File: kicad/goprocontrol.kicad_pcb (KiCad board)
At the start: 2 copper layers, 45.7 x 49.8 mm, 23 parts, among them P1 CONN_01X02, P2 CONN_01X06, Q1 IRLML6344, SW1 Reset, SW2 Prog, U1 LTV-814, U2 ESP-12E, U3 D24V5F3

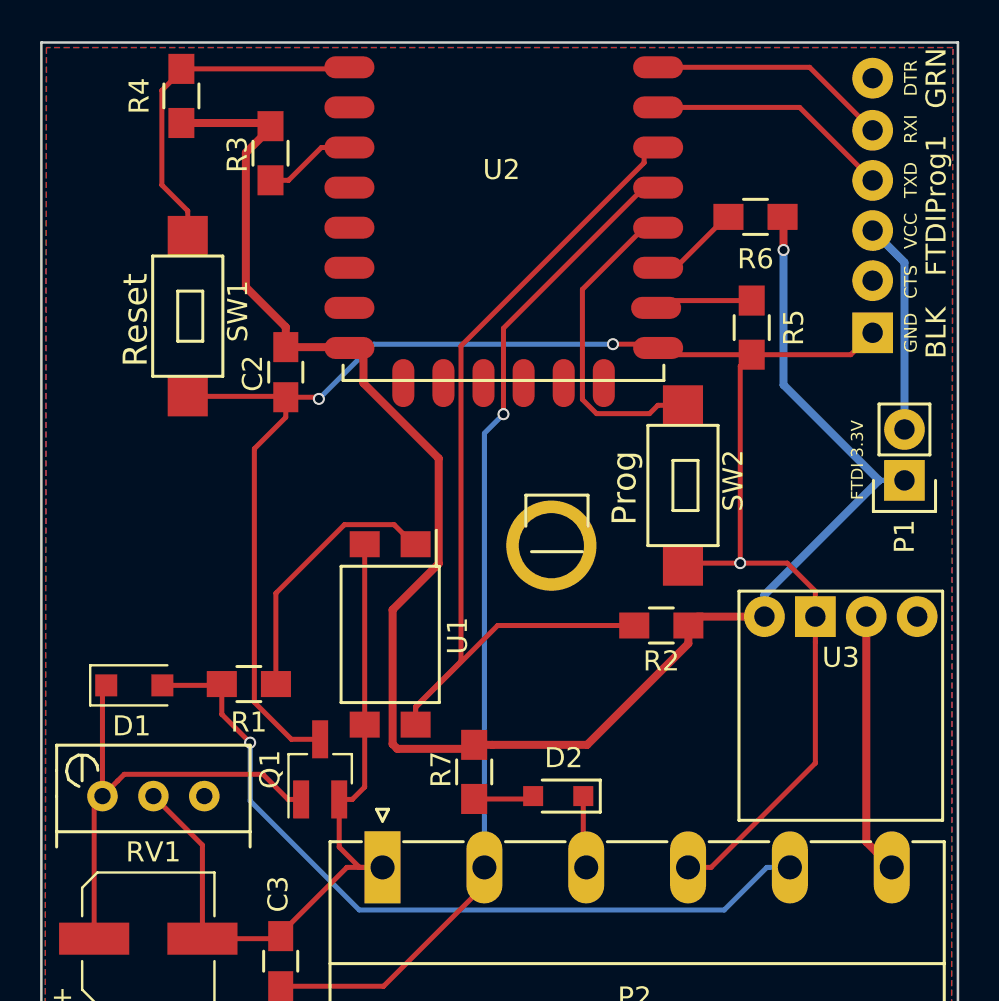
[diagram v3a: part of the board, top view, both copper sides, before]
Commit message: v2.3 Board
- Larger holes for 1x6 connector
- Move 3.3V regulator out of the way
- clean up traces
- remove 3.3V FTDI selector
- Move Prog switch
- Better GND/SW-GND for MOSFET
- Add status LED
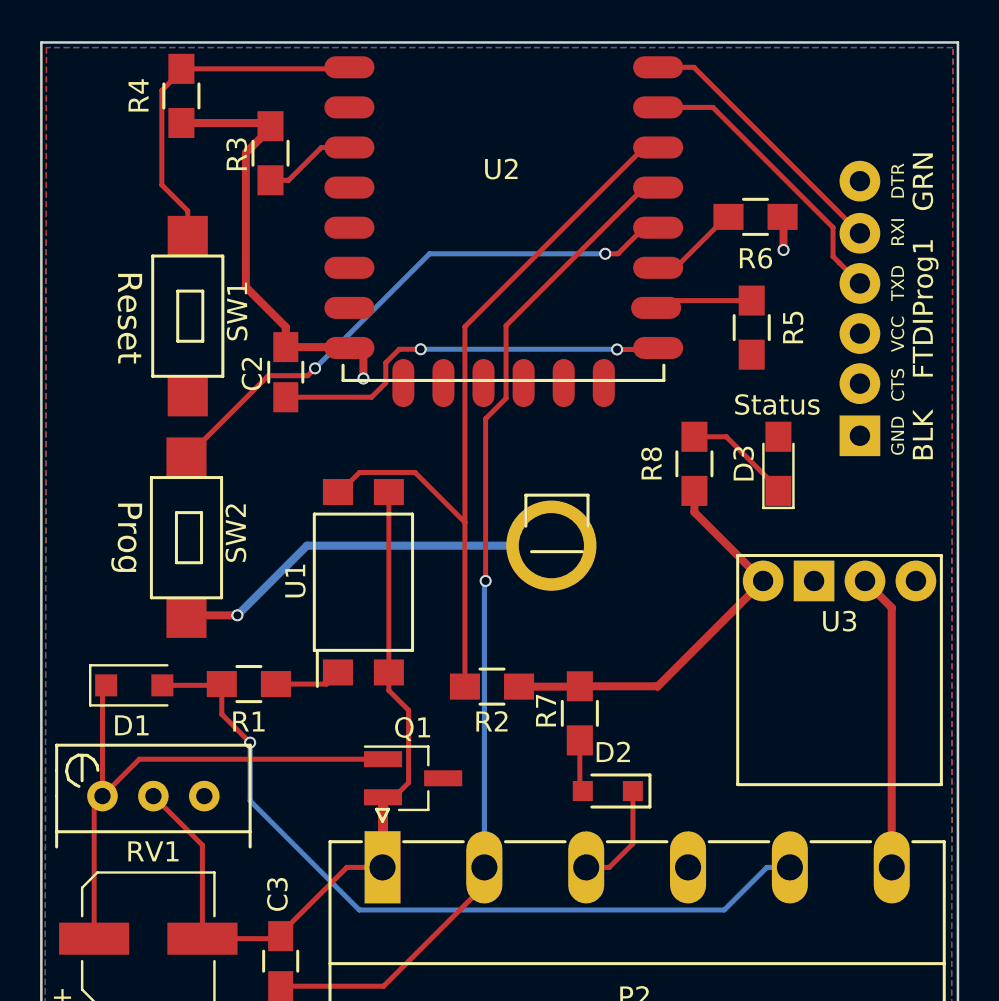
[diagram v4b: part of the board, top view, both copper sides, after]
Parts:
- removed P1: CONN_01X02, Pin_Headers:Pin_Header_Straight_1x02
- added D3: Red, LEDs:LED_0805_HandSoldering, F.Cu at (199.3, 109.9)
- added R8: 56, Resistors_SMD:R_0805_HandSoldering, F.Cu at (195.1, 109.9)
- P2: footprint Connectors_Phoenix:PhoenixContact_MC-G_06x5.08mm_Angled -> PhoenixContact_MC-G_06x5.08mm_Angled
- moved SW2 24.9 mm to (169.8, 113.6)
- moved R2 8.98 mm to (185.0, 121.0)
- moved R7 6.03 mm to (189.4, 122.4)
- moved FTDIProg1 5.18 mm to (203.4, 102.2)
- moved Q1 4.66 mm to (181.1, 125.6), turned to 0 degrees
- moved U1 2.93 mm to (178.6, 115.8), turned to 90 degrees
- moved D2 2.49 mm to (190.8, 126.2)
- moved U3 1.78 mm to (207.5, 118.3)
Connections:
- FTDIProg1 pad 4: Net-(FTDIProg1-Pad4) -> (no net)
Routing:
- net SwitchedGnd: track 91.0 -> 39.2 mm
- net +3V3: track 91.8 -> 44.2 mm, vias 1 -> 2
- net Net-(SW2-Pad1): track 15.3 -> 27.6 mm, vias 0 -> 2
- net Net-(FTDIProg1-Pad4): track 10.6 -> 0.00 mm
- net Net-(R1-Pad1): track 13.3 -> 3.34 mm
- net GPIO5: track 47.1 -> 38.5 mm
- net Net-(D3-Pad1): track 0.00 -> 5.37 mm
- net Net-(C1-Pad1): track 23.8 -> 27.6 mm
- net RXD: track 12.9 -> 15.2 mm
- net LoggerTrigger: track 3.62 -> 5.66 mm
- net +12V: track 13.0 -> 14.8 mm
- net TXD: track 12.7 -> 14.2 mm
- net GND: track 37.3 -> 38.6 mm
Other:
- board text added: "GoProControl v2.3 https://synfin.net/goprocontrol"
- board text added: "Status"
- board text removed: "FTDI 3.3V"
- board text removed: "GoProControl v2.2 https://synfin.net/goprocontrol"

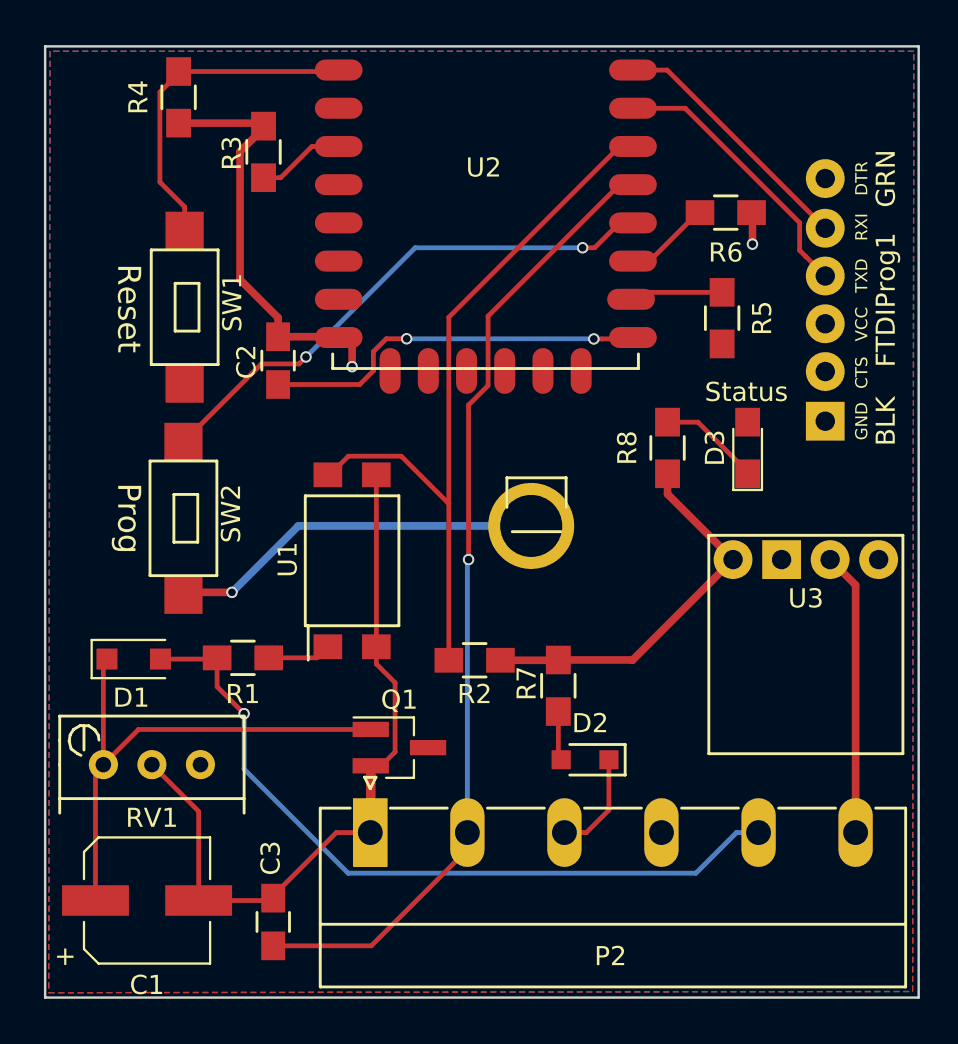
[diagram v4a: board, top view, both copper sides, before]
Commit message: v2.5 of the board
- Move main connector to front
- Use MOSFET to drive GPIO12 like MXL2
- Larger traces for Switched Ground
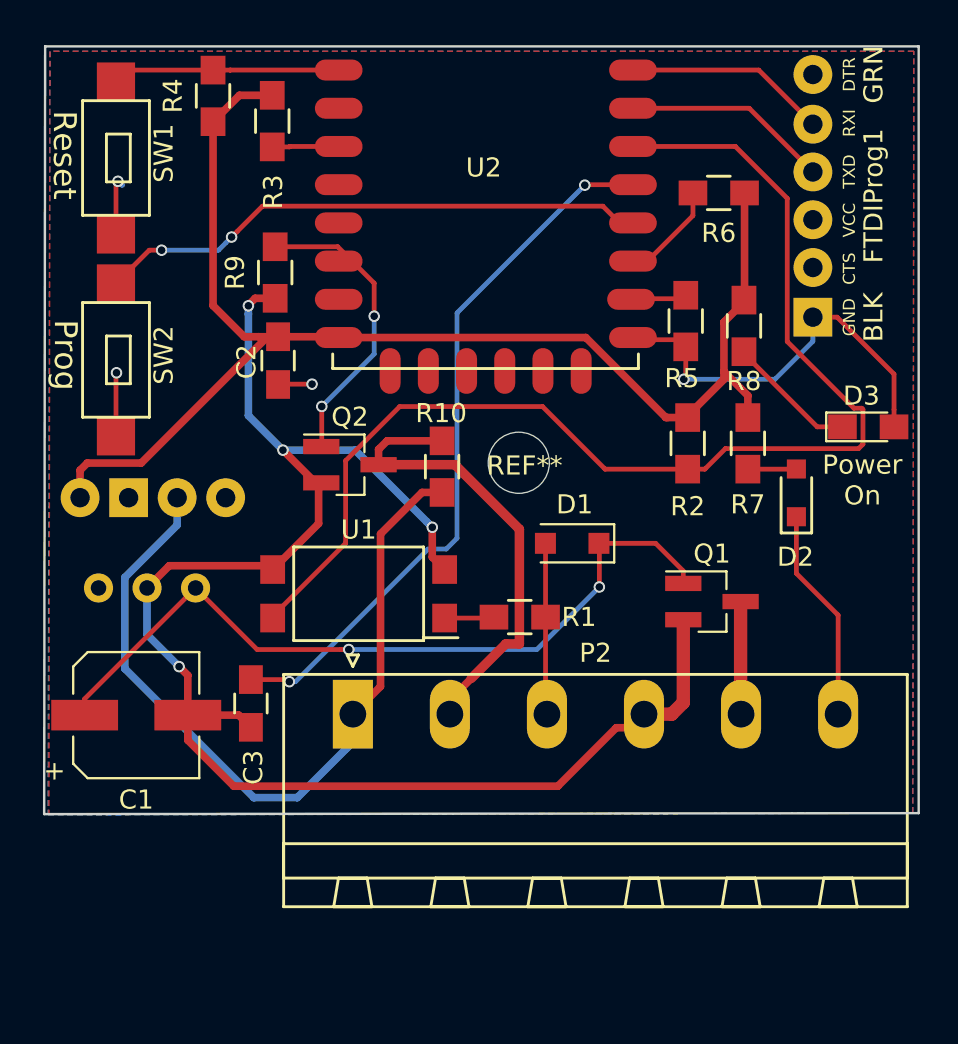
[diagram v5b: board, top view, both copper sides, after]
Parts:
- removed ?: Pin_Header_Straight_1x01, Pin_Headers:Pin_Header_Straight_1x01
- added Q2: IRLML6344, TO_SOT_Packages_SMD:SOT-23_Handsoldering, F.Cu at (178.5, 110.8)
- added R10: 10K, Resistors_SMD:R_0805_HandSoldering, F.Cu at (183.3, 110.9)
- added R9: 10K, Resistors_SMD:R_0805_HandSoldering, F.Cu at (174.6, 100.7)
- added REF**: MountingHole_3.2mm_M3, Mounting_Holes:MountingHole_3.2mm_M3, F.Cu at (187.4, 110.7)
- P2: footprint PhoenixContact_MC-G_06x5.08mm_Angled -> Connectors_Phoenix:PhoenixContact_MSTBA-G_06x5.08mm_Angled
- RV1, U3: moved to B.Cu
- moved U3 35.2 mm to (173.3, 110.0)
- moved D1 23.7 mm to (190.1, 114.9), turned to 180 degrees
- moved Q1 18.1 mm to (197.5, 118.0)
- moved D2 17.8 mm to (201.9, 112.3), turned to 90 degrees
- moved R7 16.1 mm to (199.3, 109.7)
- moved R2 15.9 mm to (196.2, 109.7), turned to 270 degrees
- moved R1 14.6 mm to (187.4, 118.8), turned to 0 degrees
- moved C3 11.5 mm to (173.3, 123.3), turned to 270 degrees
- moved RV1 10.4 mm to (170.4, 117.2)
- moved C1 9.72 mm to (167.3, 123.9)
- moved SW2 9.01 mm to (166.3, 105.3)
- moved SW1 8.60 mm to (166.3, 94.7)
- moved R8 7.54 mm to (199.1, 103.5), turned to 270 degrees
- moved D3 6.41 mm to (205.6, 108.8), turned to 0 degrees
- moved P2 6.26 mm to (178.7, 123.9)
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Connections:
- P2 pad 1: GND -> +12V
- P2 pad 2: GPIO4 -> GPIO12-OUT
- P2 pad 3: LoggerTrigger -> Switched12V
- P2 pad 4: SwitchedGnd -> GND
- P2 pad 5: Switched12V -> SwitchedGnd
- P2 pad 6: +12V -> LoggerTrigger
- U2 pad 6: (no net) -> GPIO12
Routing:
- net GND: track 38.6 -> 84.1 mm, vias 0 -> 4
- net Switched12V: track 39.5 -> 9.08 mm, vias 1 -> 0
- net +12V: track 14.8 -> 42.1 mm
- net +3V3: track 44.2 -> 71.2 mm, vias 2 -> 0
- net GPIO5: track 38.5 -> 64.7 mm
- net GPIO12-OUT: track 0.00 -> 24.7 mm
- net GPIO12: track 0.00 -> 15.7 mm, vias 0 -> 2
- net Net-(C1-Pad1): track 27.6 -> 40.8 mm, vias 0 -> 2
- net GPIO4: track 50.4 -> 38.2 mm, vias 1 -> 2
- net LoggerTrigger: track 5.66 -> 11.9 mm
- net Net-(R4-Pad2): track 18.4 -> 12.6 mm
- net RXD: track 15.2 -> 11.5 mm
- net TXD: track 14.2 -> 11.3 mm
- net SwitchedGnd: track 39.2 -> 36.7 mm, vias 3 -> 4
- net Net-(R5-Pad1): track 5.52 -> 3.55 mm
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- added copper zone on B.Cu, net SwitchedGnd
- removed copper zone on B.Cu, net +3V3
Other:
- board size 45.7 x 49.8 mm -> 45.8 x 40.2 mm
- net class GPIO12-OUT added: clearance 0.2, trace_width 0.4, via_dia 0.6, via_drill 0.4
- board text added: "GPIO12"
- board text added: "GoProControl v2.5 https://synfin.net/goprocontrol 20180318"
- board text added: "Power On"
- board text added: "Sw12V"
- board text added: "SwGND"
- board text removed: "20180218"
- board text removed: "GPIO4"
- board text removed: "GoProControl v2.3 https://synfin.net/goprocontrol"
- board text removed: "Status"
- board text removed: "Switched 12V"
- board text removed: "Switched GND"
